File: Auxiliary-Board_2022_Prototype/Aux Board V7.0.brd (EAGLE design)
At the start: 237.2 x 97.8 mm, 47 parts, among them CON11 1X01, CON12 1X01, CON13 1X01, CON14 1X01, CON15 1X01, CON16 1X01, CON17 1X01, CON18 1X01, CON5 1X01, CON8 1X01

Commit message: feat: add mechanical relay and 6-pin,2-pin te connectors
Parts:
- removed AUX_PWR2: 5555140-6, 5555140-6 RJ11:1734723-1_RJ11
- removed ISP_328P1, ISP_328P3: ISP, EcoCar-Microcontrollers:ISP_CONNECTOR
- removed LED_328P, SERVO_328P3: 328P, EcoCar-Microcontrollers:DIP28
- removed PB1, PB3: (no value), EcoCar-Electromechanical:PUSHBUTTON
- removed Q5: (no value), EcoCar-Discrete-Semiconductors:TO-263/D2PAK
- removed R1, R12: 10K, EcoCar-Passives:0805
- removed R8: 0, EcoCar-Passives:0805
- removed SGNL_BACK, SGNL_FRONT: TE_4-PIN, EcoCar-Connectors:TE_4-PIN
- added AUX_PWR_IN: TE_6-PIN, EcoCar-Connectors:TE_6-PIN
- added K1: RELAY_SPST-NO_3A, EcoCar-Electromechanical:TE_1-1721081-2
- added SGNL_BACK_LEFT, SGNL_BACK_RIGHT, SGNL_FRONT_LEFT, SGNL_FRONT_RIGHT: TE_2-PIN, EcoCar-Connectors:TE_2-PIN
- renumbered 12V_AUX_IN to 12V_BACKUP, 5V_AUX_IN to 5V_BACKUP, BRK to BRK_PWR, SERVO to SERVO_PWR
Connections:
- removed net MISO_328P1: ISP_328P1.1, LED_328P.18
- removed net MISO_328P3: ISP_328P3.1, SERVO_328P3.18
- removed net MOSI_328P1: ISP_328P1.4, LED_328P.17
- removed net MOSI_328P3: ISP_328P3.4, SERVO_328P3.17
- removed net RESET_328P1: ISP_328P1.5, LED_328P.1, PB1.1, PB1.2, R1.2
- removed net RESET_328P3: ISP_328P3.5, PB3.1, PB3.2, R12.2, SERVO_328P3.1
- removed net SCK_328P1: ISP_328P1.3, LED_328P.19
- removed net SCK_328P3: ISP_328P3.3, SERVO_328P3.19
- net 12V: now also AUX_PWR_IN.4, AUX_PWR_IN.6, K1.3; no longer AUX_PWR2.2, AUX_PWR2.5, R8.2, SGNL_BACK.1, SGNL_FRONT.1
- net 5V: now also AUX_PWR_IN.1, AUX_PWR_IN.3; no longer AUX_PWR2.3, AUX_PWR2.4, ISP_328P1.2, ISP_328P3.2, LED_328P.7, R1.1, R12.1, SERVO_328P3.7
- net BRK_12V: now also K1.4; no longer Q5.2, R8.1
- net BRK_O/P: no longer LED_328P.13, Q5.1
- net GND: now also AUX_PWR_IN.2, AUX_PWR_IN.5, SGNL_BACK_LEFT.2, SGNL_BACK_RIGHT.2, SGNL_FRONT_LEFT.2, SGNL_FRONT_RIGHT.2; no longer AUX_PWR2.1, AUX_PWR2.6, AUX_PWR2.SH1, AUX_PWR2.SH2, ISP_328P1.6, ISP_328P3.6, LED_328P.22, LED_328P.8, PB1.3, PB1.4, PB3.3, PB3.4, Q5.3, SERVO_328P3.22, SERVO_328P3.8, SGNL_BACK.4, SGNL_FRONT.4
- net HAZARD_I/P: no longer LED_328P.5
- net LEFT_I/P: no longer LED_328P.28
- net LEFT_O/P: no longer LED_328P.4
- net RIGHT_I/P: no longer LED_328P.27
- net RIGHT_O/P: no longer LED_328P.14
- net SERVO_I/P: no longer SERVO_328P3.12
- net SERVO_O/P: no longer SERVO_328P3.13
- net SGNL_LEFT_12V: now also SGNL_BACK_LEFT.1, SGNL_FRONT_LEFT.1; no longer SGNL_BACK.3, SGNL_FRONT.3
- net SGNL_RIGHT_12V: now also SGNL_BACK_RIGHT.1, SGNL_FRONT_RIGHT.1; no longer SGNL_BACK.2, SGNL_FRONT.2

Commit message: feat: finish schematic and initial board route
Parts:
- removed BRK_328P2: 328P, EcoCar-Microcontrollers:DIP28
- removed K1: RELAY_SPST-NO_3A, EcoCar-Electromechanical:TE_1-1721081-2
- removed PANEL_IN: RJ45, EcoCar-Connectors:RJ45
- removed R5, R6: 0, EcoCar-Passives:0805
- removed SGNL_BACK_LEFT, SGNL_BACK_RIGHT, SGNL_FRONT_LEFT, SGNL_FRONT_RIGHT: TE_2-PIN, EcoCar-Connectors:TE_2-PIN
- added AVCC_JMP: (no value), EcoCar-Passives:JUMPER-0.45
- added BRK_LIGHT_RELAY: RELAY_SPST-NO_3A, EcoCar-Electromechanical:TE_1-1721081-2
- added CENTER_CONSOLE: RJ45, EcoCar-Connectors:RJ45
- added MCU_328P2: 328P, EcoCar-Microcontrollers:DIP28
- added R1: 1K, EcoCar-Passives:0805
- added SGNL_BCK_LFT, SGNL_BCK_RT, SGNL_FRNT_LFT, SGNL_FRNT_RT: TE_2-PIN, EcoCar-Connectors:TE_2-PIN
- moved 12V_BACKUP 236.6 mm to (2.54, 54.4), turned to 270 degrees
- moved 5V_BACKUP 222.3 mm to (2.54, 31.5), turned to 270 degrees
- moved C4 203.4 mm to (14.4, 69.5), flipped to the bottom, turned to 180 degrees
- moved C5 200.0 mm to (14.4, 65.7), flipped to the bottom, turned to 180 degrees
- moved C6 196.6 mm to (14.4, 61.8), flipped to the bottom, turned to 180 degrees
- moved H3 181.2 mm to (104.1, 15.2)
- moved H1 151.1 mm to (104.1, 91.4)
- moved AUX_PWR_IN 144.3 mm to (7.62, 78.7), turned to 270 degrees
- moved CON16 131.4 mm to (20.3, 21.6)
- moved CON17 131.4 mm to (16.5, 21.6)
- moved CON18 131.4 mm to (12.7, 21.6)
- moved Q1 122.3 mm to (76.2, 52.1), turned to 0 degrees
- moved Q4 117.2 mm to (57.1, 74.9), turned to 0 degrees
- moved SERVO_PWR 110.0 mm to (33.0, 100.3), turned to 180 degrees
- moved H4 108.7 mm to (10.2, 15.2)
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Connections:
- removed net LEFT_I/P: STEERING-WHEEL.1
- removed net LEFT_O/P: Q1.1
- removed net RIGHT_I/P: STEERING-WHEEL.2
- removed net RIGHT_O/P: Q4.1
- new net N$1: BRK_LIGHT_RELAY.1, R1.1
- new net N$2: AVCC_JMP.P$2, MCU_328P2.20
- new net SERVO_ADC_I/P: MCU_328P2.27, STEERING-WHEEL.2
- new net SGNL_LEFT_I/P: MCU_328P2.25, STEERING-WHEEL.6
- new net SGNL_LEFT_O/P: MCU_328P2.12, Q1.1
- new net SGNL_RIGHT_I/P: MCU_328P2.26, STEERING-WHEEL.8
- new net SGNL_RIGHT_O/P: MCU_328P2.15, Q4.1
- net 12V: now also BRK_LIGHT_RELAY.3, SGNL_BCK_LFT.1, SGNL_BCK_RT.1, SGNL_FRNT_LFT.1, SGNL_FRNT_RT.1; no longer K1.3, R5.2, R6.2
- net 5V: now also AVCC_JMP.P$1, MCU_328P2.7; no longer BRK_328P2.7, PANEL_IN.5, STEERING-WHEEL.3, STEERING-WHEEL.4
- net BRK_12V: now also BRK_LIGHT_RELAY.4; no longer K1.4
- net BRK_I/P: now also CENTER_CONSOLE.8, MCU_328P2.24; no longer BRK_328P2.12, PANEL_IN.4
- net BRK_O/P: now also BRK_LIGHT_RELAY.2, MCU_328P2.23; no longer BRK_328P2.13
- net GND: now also CENTER_CONSOLE.10, CENTER_CONSOLE.9, MCU_328P2.22, MCU_328P2.8, R1.2; no longer BRK_328P2.22, BRK_328P2.8, PANEL_IN.10, PANEL_IN.8, PANEL_IN.9, SGNL_BACK_LEFT.2, SGNL_BACK_RIGHT.2, SGNL_FRONT_LEFT.2, SGNL_FRONT_RIGHT.2
- net HAZARD_I/P: now also CENTER_CONSOLE.6, MCU_328P2.6; no longer PANEL_IN.2
- net MISO_328P2: now also MCU_328P2.18; no longer BRK_328P2.18
- net MOSI_328P2: now also MCU_328P2.17; no longer BRK_328P2.17
- net RESET_328P2: now also MCU_328P2.1; no longer BRK_328P2.1
- net SCK_328P2: now also MCU_328P2.19; no longer BRK_328P2.19
- net SERVO_I/P: now also MCU_328P2.4, STEERING-WHEEL.4; no longer PANEL_IN.1
- net SGNL_LEFT_12V: now also SGNL_BCK_LFT.2, SGNL_FRNT_LFT.2; no longer R5.1, SGNL_BACK_LEFT.1, SGNL_FRONT_LEFT.1
- net SGNL_RIGHT_12V: now also SGNL_BCK_RT.2, SGNL_FRNT_RT.2; no longer R6.1, SGNL_BACK_RIGHT.1, SGNL_FRONT_RIGHT.1
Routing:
- net 12V: track 26.8 -> 288.0 mm
- net 5V: track 0.00 -> 122.4 mm
- net HAZARD_I/P: track 0.00 -> 114.4 mm
- net BRK_I/P: track 0.00 -> 90.9 mm
- net SGNL_LEFT_I/P: track 0.00 -> 87.7 mm
- net SERVO_ADC_I/P: track 0.00 -> 81.8 mm
- net SGNL_RIGHT_I/P: track 0.00 -> 81.5 mm
- net SGNL_RIGHT_12V: track 0.00 -> 79.0 mm
- net RESET_328P2: track 0.00 -> 75.9 mm
- net SGNL_LEFT_12V: track 0.00 -> 75.4 mm
- net SERVO_I/P: track 0.00 -> 70.1 mm
- net SGNL_LEFT_O/P: track 0.00 -> 43.4 mm
- net SCK_328P2: track 0.00 -> 32.4 mm
- net SGNL_RIGHT_O/P: track 0.00 -> 26.2 mm
- net N$1: track 0.00 -> 24.8 mm
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- added copper zone on layer 1, net GND
- added copper zone on layer 16, net GND
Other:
- board size 237.2 x 97.8 mm -> 114.3 x 96.6 mm

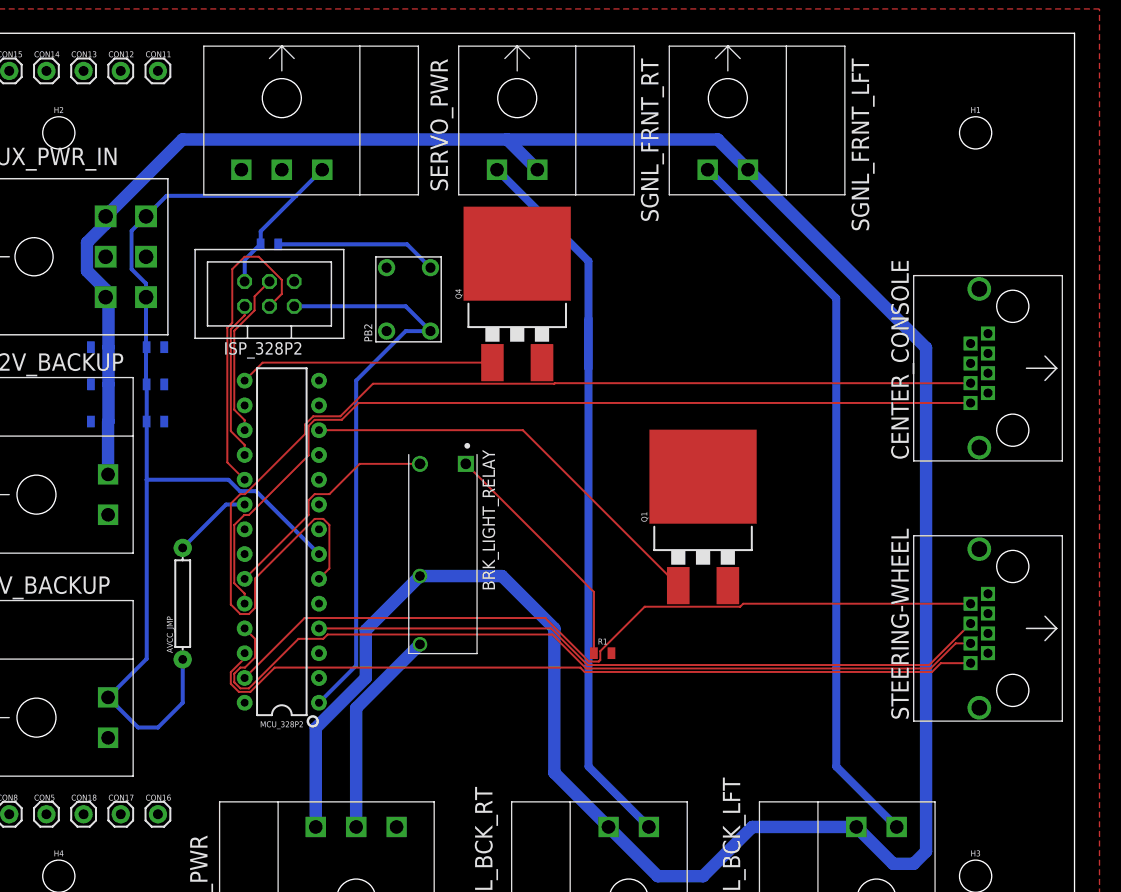
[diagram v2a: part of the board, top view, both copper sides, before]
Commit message: feat: rework board, add pwr LEDs, add decoupling caps, add flyback diode
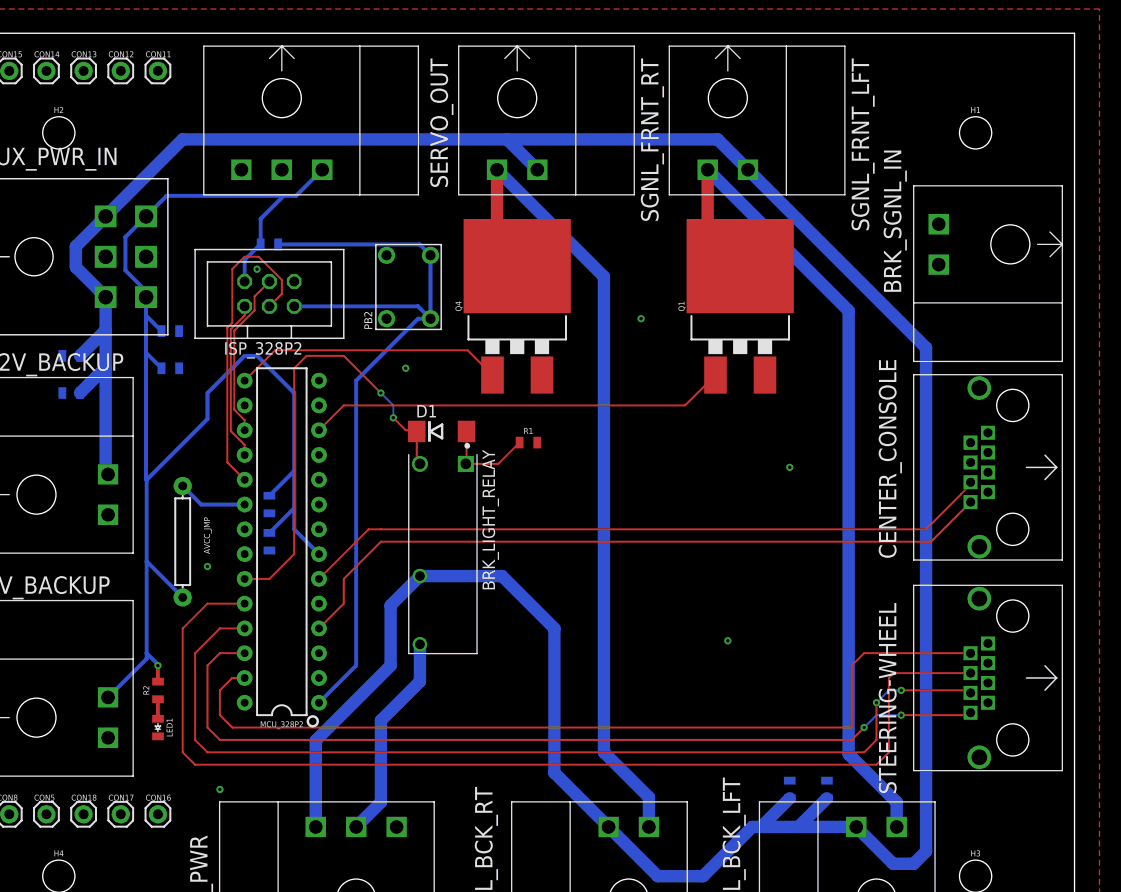
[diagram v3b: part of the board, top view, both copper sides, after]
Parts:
- added BRK_SGNL_IN: TE_2-PIN, EcoCar-Connectors:TE_2-PIN
- added C7: 10n, EcoCar-Passives:0805
- added C8: 0.1u, EcoCar-Passives:0805
- added D1: (no value), EcoCar-Discrete-Semiconductors:DO214AA
- added LED1: (no value), EcoCar-Discrete-Semiconductors:0805_LED
- added R2: 2K, EcoCar-Passives:0805
- C1: value 10u -> 0.1u
- C4, C5: value 10n -> 0.1u
- C6: value 10u -> 10n
- moved C6 83.5 mm to (88.9, 24.1), turned to 270 degrees
- moved R1 22.9 mm to (58.3, 59.7)
- moved Q1 21.9 mm to (80.0, 73.7)
- moved C2 19.9 mm to (31.8, 49.5), turned to 90 degrees
- moved C1 14.5 mm to (31.8, 53.3), turned to 90 degrees
- moved CENTER_CONSOLE 10.2 mm to (108.0, 50.8)
- moved C4 7.55 mm to (21.6, 67.3), turned to 0 degrees
- moved AVCC_JMP 6.35 mm to (22.9, 49.5)
- moved STEERING-WHEEL 5.08 mm to (108.0, 29.2)
- moved C5 3.05 mm to (11.4, 64.8)
- moved C3 2.25 mm to (21.6, 71.1)
- moved Q4 1.27 mm to (57.1, 73.7)
- moved PB2 1.27 mm to (48.3, 72.4)
- renumbered SERVO_PWR to SERVO_OUT
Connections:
- new net N$8: LED1.1, R2.1
- net 12V: now also C7.2, C8.2; no longer C4.2
- net 5V: now also C4.2, R2.2
- net BRK_I/P: now also BRK_SGNL_IN.1, MCU_328P2.4; no longer MCU_328P2.24
- net BRK_O/P: now also D1.C
- net GND: now also BRK_SGNL_IN.2, C7.1, C8.1, LED1.2
- net N$1: now also D1.A
- net SERVO_I/P: now also MCU_328P2.24; no longer MCU_328P2.4
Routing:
- net HAZARD_I/P: track 114.4 -> 71.0 mm
- net SERVO_I/P: track 70.1 -> 109.8 mm
- net 5V: track 122.4 -> 144.6 mm, vias 0 -> 1
- net BRK_O/P: track 23.7 -> 45.7 mm, vias 0 -> 2
- net BRK_I/P: track 90.9 -> 73.7 mm, vias 0 -> 1
- net 12V: track 288.0 -> 304.9 mm
- net N$1: track 24.8 -> 9.77 mm
- net SGNL_LEFT_I/P: track 87.7 -> 100.0 mm, vias 0 -> 2
- net SGNL_RIGHT_I/P: track 81.5 -> 90.6 mm, vias 0 -> 2
- net SGNL_LEFT_12V: track 75.4 -> 83.9 mm
- net SERVO_ADC_I/P: track 81.8 -> 90.0 mm
- net RESET_328P2: track 75.9 -> 81.9 mm
- net SGNL_RIGHT_12V: track 79.0 -> 84.6 mm
- net N$8: track 0.00 -> 2.01 mm
- net SGNL_RIGHT_O/P: track 26.2 -> 27.7 mm
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
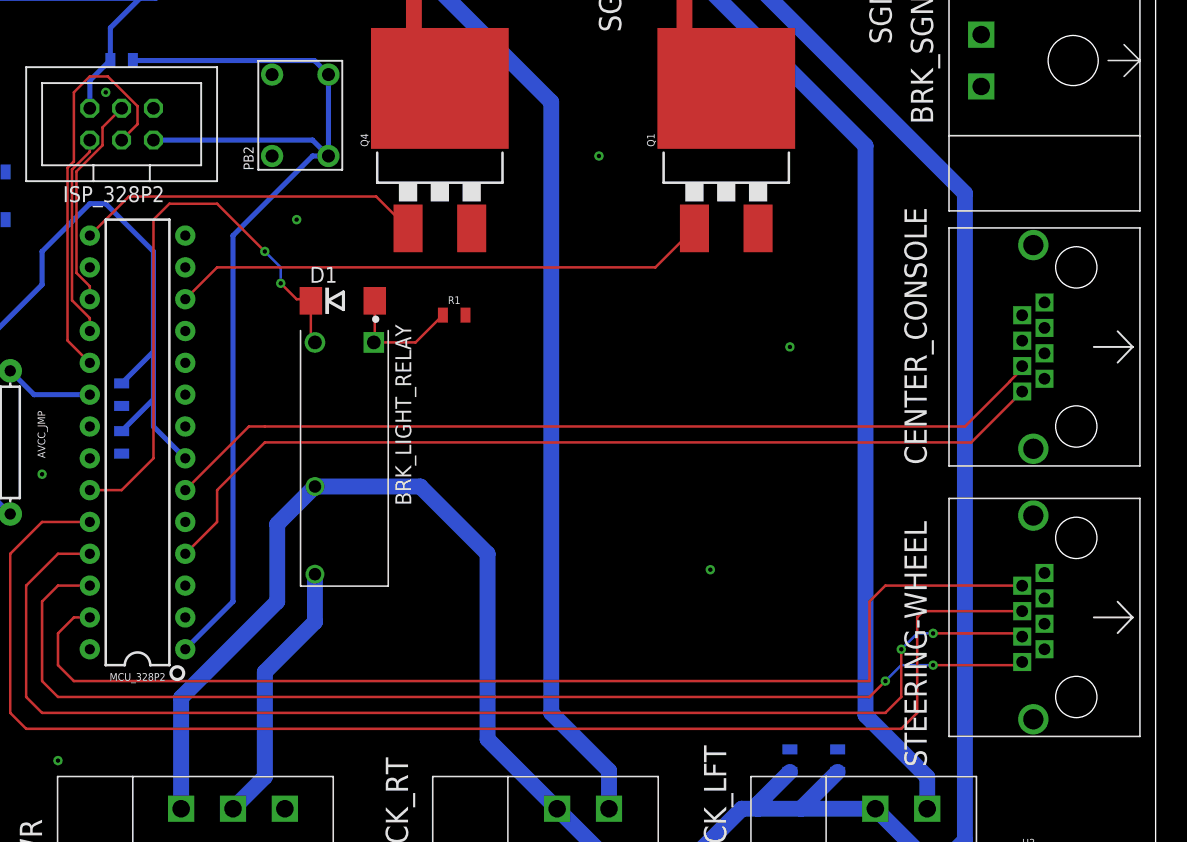
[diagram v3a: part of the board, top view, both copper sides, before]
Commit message: feat: add RS232 partially, change inputs to one RJ45 port
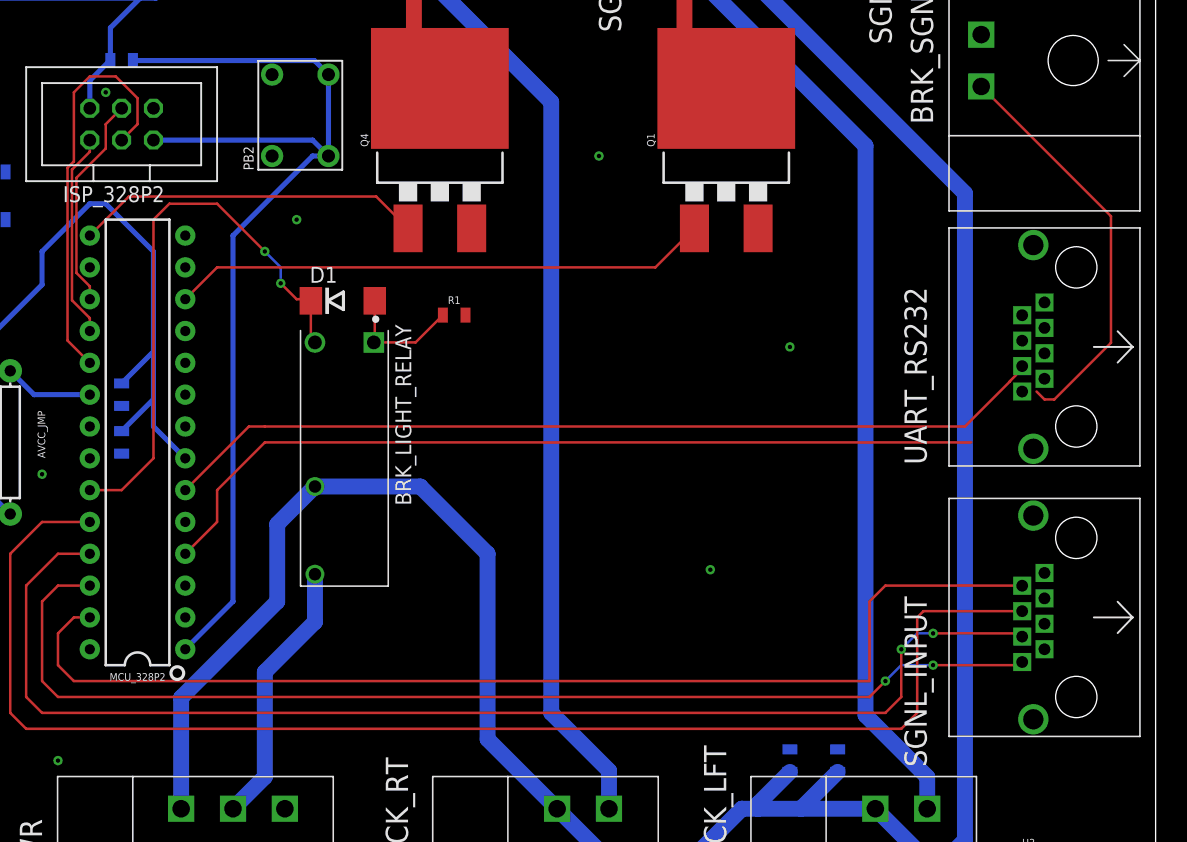
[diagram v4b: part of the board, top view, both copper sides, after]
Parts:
- renumbered CENTER_CONSOLE to UART_RS232, STEERING-WHEEL to SGNL_INPUT
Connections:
- new net RS_RX: UART_RS232.5
- new net RS_TX: UART_RS232.2
- net BRK_I/P: now also SGNL_INPUT.7; no longer UART_RS232.8
- net GND: now also UART_RS232.3, UART_RS232.4
- net HAZARD_I/P: now also SGNL_INPUT.1; no longer UART_RS232.6
- net SERVO_O/P: now also MCU_328P2.28
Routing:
- net BRK_I/P: track 73.7 -> 100.7 mm, vias 1 -> 0
